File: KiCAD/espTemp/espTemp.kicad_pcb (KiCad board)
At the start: 2 copper layers, 38.1 x 25.4 mm, 7 parts, among them U1 ESP-01, U2 LD1117S33TR_SOT223, U3 DHT11

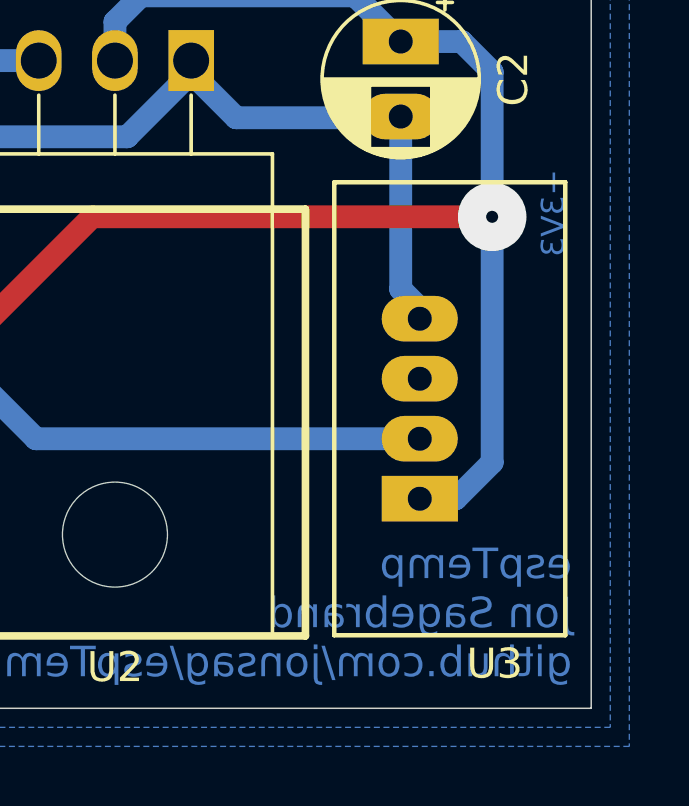
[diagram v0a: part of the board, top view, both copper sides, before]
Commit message: now dht22
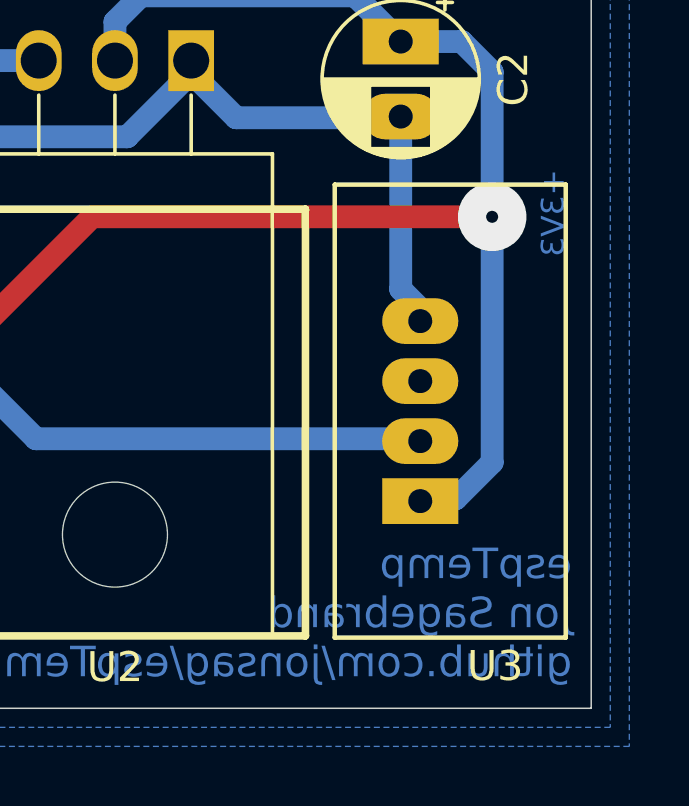
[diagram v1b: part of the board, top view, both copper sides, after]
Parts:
- U3: value DHT11 -> DHT22,CM2303
- moved U3 0.08 mm to (165.5, 88.5)
